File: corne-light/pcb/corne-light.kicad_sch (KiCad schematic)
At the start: 43 parts, among them SW22 SW_PUSH, SW23 SW_PUSH, SW24 SW_PUSH, SW25 SW_PUSH, SW26 SW_PUSH, SW27 SW_PUSH, SW28 SW_PUSH, SW29 SW_PUSH, SW30 SW_PUSH, SW31 SW_PUSH, SW32 SW_PUSH, SW33 SW_PUSH, SW34 SW_PUSH, SW35 SW_PUSH, SW36 SW_PUSH, SW37 SW_PUSH, SW38 SW_PUSH, SW39 SW_PUSH, SW40 SW_PUSH, SW41 SW_PUSH, SW42 SW_PUSH, U1 nice_nano

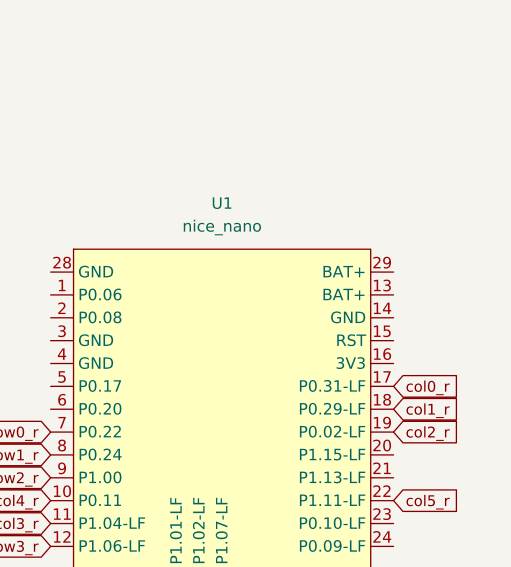
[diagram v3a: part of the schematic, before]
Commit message: Improve clearances
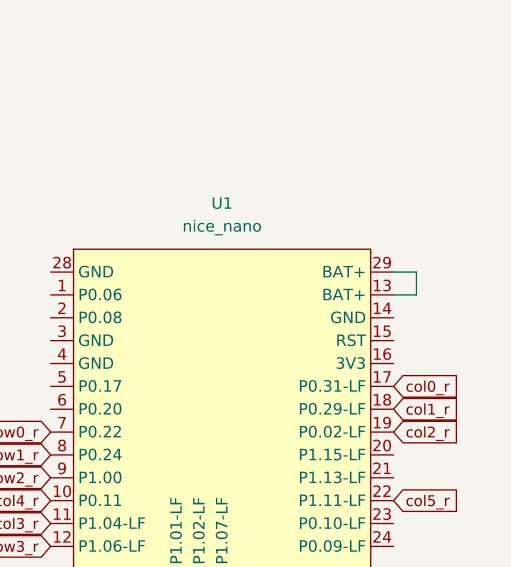
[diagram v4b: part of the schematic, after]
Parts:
- D27, D33: footprint Diode_THT:D_DO-35_SOD27_P10.16mm_Horizontal -> Diode_THT:D_DO-35_SOD27_P7.62mm_Horizontal
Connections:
- net at U1.13 (BAT+): now also U1.29 (BAT+)
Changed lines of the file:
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@@
+	(wire
+		(pts
+			(xy 184.15 49.53) (xy 186.69 49.53)
+		)
+		(stroke
+			(width 0)
+			(type default)
+		)
+	)
 	(wire
 		(pts
@@
 	(wire
 		(pts
+			(xy 186.69 49.53) (xy 186.69 52.07)
+		)
+		(stroke
+			(width 0)
+			(type default)
+		)
+	)
+	(wire
+		(pts
 			(xy 69.85 137.16) (xy 69.85 144.78)
 		)
@@
 		(pts
 			(xy 153.67 106.68) (xy 153.67 121.92)
+		)
+		(stroke
+			(width 0)
+			(type default)
+		)
+	)
+	(wire
+		(pts
+			(xy 186.69 52.07) (xy 184.15 52.07)
 		)
 		(stroke
@@
 			)
 		)
-		(property "Footprint" "Diode_THT:D_DO-35_SOD27_P10.16mm_Horizontal"
+		(property "Footprint" "Diode_THT:D_DO-35_SOD27_P7.62mm_Horizontal"
 			(at 157.48 106.68 0)
 			(effects
@@
 			)
 		)
-		(property "Footprint" "Diode_THT:D_DO-35_SOD27_P10.16mm_Horizontal"
+		(property "Footprint" "Diode_THT:D_DO-35_SOD27_P7.62mm_Horizontal"
 			(at 157.48 121.92 0)
 			(effects
